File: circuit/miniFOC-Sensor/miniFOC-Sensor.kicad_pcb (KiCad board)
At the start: 2 copper layers, 0 parts

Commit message: Completed PCB drawing of miniFOC sensor board
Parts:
- added C1: 100nF, Capacitor_SMD:C_0402_1005Metric, B.Cu at (154.7, 105.8)
- added C2: 22uF, Capacitor_SMD:C_0603_1608Metric, F.Cu at (150.4, 107.0)
- added C3: 22uF, Capacitor_SMD:C_0603_1608Metric, B.Cu at (154.7, 102.3)
- added J1: Conn_01x05, Connector_JST:JST_GH_SM05B-GHS-TB_1x05-1MP_P1.25mm_Horizontal, F.Cu at (149.8, 115.6)
- added U1: MT6701, Package_SO:SOP-8_3.9x4.9mm_P1.27mm, B.Cu at (149.8, 104.3)
- added U2: XC6206P332MR, Package_TO_SOT_SMD:SOT-23, F.Cu at (149.8, 104.3)
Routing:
- net /SPI_CS: track 0.00 -> 14.3 mm, vias 0 -> 1
- net +5V: track 0.00 -> 13.0 mm
- net /SPI_CLK: track 0.00 -> 12.1 mm, vias 0 -> 1
- net /SPI_MISO: track 0.00 -> 9.94 mm, vias 0 -> 1
- net +3.3V: track 0.00 -> 9.25 mm, vias 0 -> 1
- net GND: vias 0 -> 8
- added copper zone on B.Cu, net GND
- added copper zone on F.Cu, net GND
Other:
- board outline added: 30 x 29 mm
- board text added: "0"
- board text added: "0 mm"
- board text added: "0.01 mm"
- board text added: "0.02"
- board text added: "0.035 mm"
- board text added: "0.2000 mm / 0.2000 mm"
- board text added: "0.3000 mm"
- board text added: "0.91 mm"
- board text added: "1"
- board text added: "1.0000 mm"
- board text added: "2"
- board text added: "29.9726 mm x 28.9824 mm"
- board text added: "3.3"
- board text added: "4.2"
- board text added: "B.Cu"
- board text added: "B.Mask"
- board text added: "B.Paste"
- board text added: "B.Silkscreen"
- board text added: "BOARD CHARACTERISTICS"
- board text added: "Black"
- board text added: "Bottom Silk Screen"
- board text added: "Bottom Solder Mask"
- board text added: "Bottom Solder Paste"
- board text added: "Epsilon R（相对介电常数）"
- board text added: "F.Cu"
- board text added: "F.Mask"
- board text added: "F.Paste"
- board text added: "F.Silkscreen"
- board text added: "FR4"
- board text added: "JLCJLCJLCJLC"
- board text added: "Loss Tangent（损耗角正切）"
- board text added: "None"
- board text added: "Not specified"
- board text added: "Top Silk Screen"
- board text added: "Top Solder Mask"
- board text added: "Top Solder Paste"
- board text added: "White"
- board text added: "copper"
- board text added: "core"
- board text added: "github.com/zhuyan zhen1/minifoc"
- board text added: "miniFOC"
- board text added: "否"
- board text added: "孔最小直径："
- board text added: "层名称"
- board text added: "最小布线/间距："
- board text added: "材料"
- board text added: "板子整体尺寸："
- board text added: "电介质"
- board text added: "电路板厚度："
- board text added: "电镀板边："
- board text added: "类型"
- board text added: "粗细 (mm)"
- board text added: "边缘卡连接器："
- board text added: "邮票孔："
- board text added: "铜层数量："
- board text added: "铜表面处理（镀铜）："
- board text added: "阻抗控制"
- board text added: "颜色"

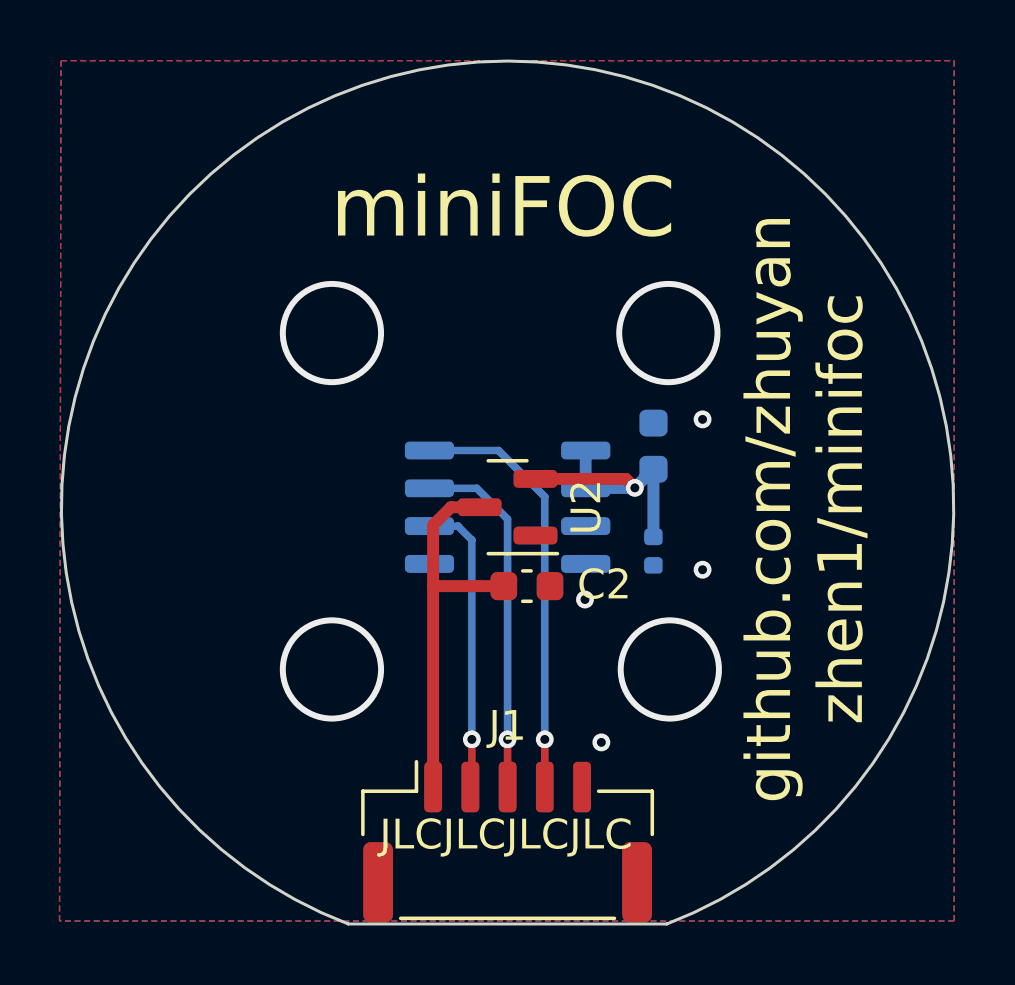
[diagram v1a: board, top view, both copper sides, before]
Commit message: Complete the circuit and PCB design for version 2.0.
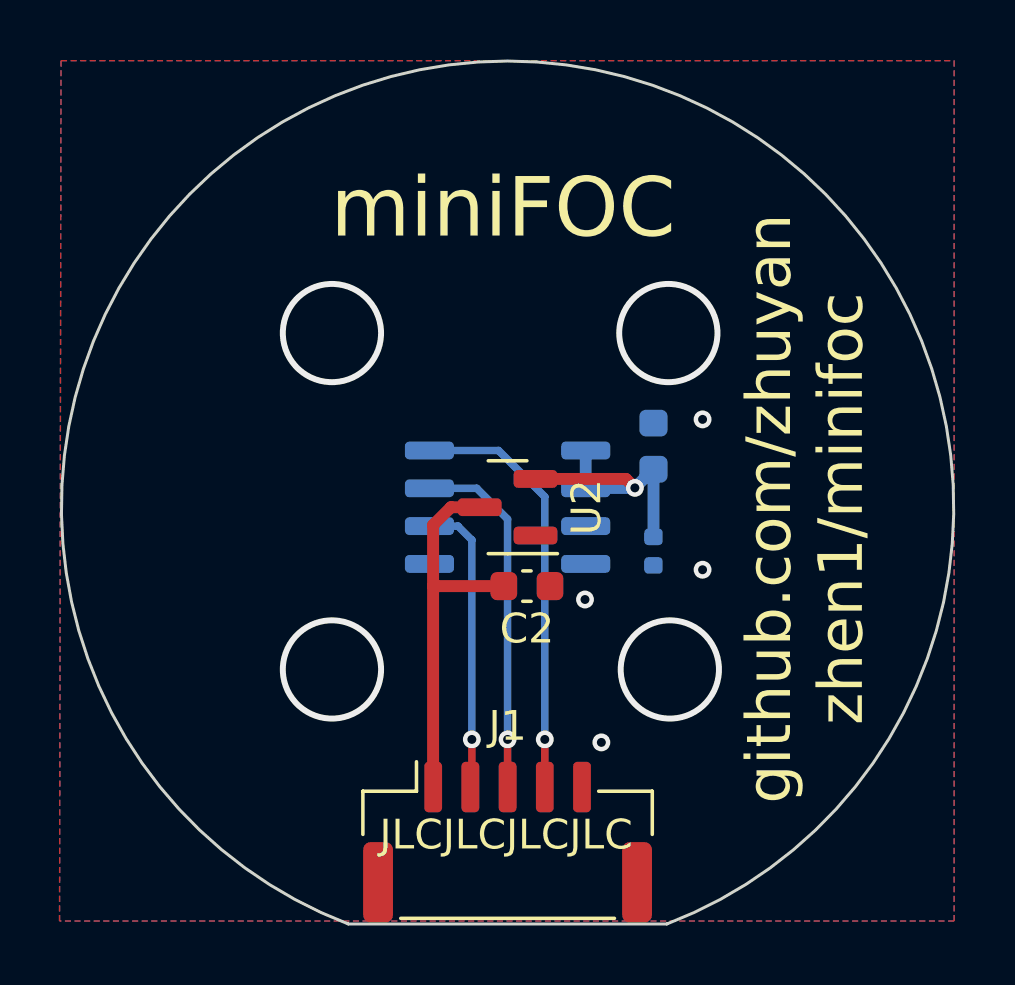
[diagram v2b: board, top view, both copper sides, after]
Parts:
- C1: footprint Capacitor_SMD:C_0402_1005Metric -> Library:C_0402_1005Metric
- C2, C3: footprint Capacitor_SMD:C_0603_1608Metric -> Library:C_0603_1608Metric
- J1: footprint Connector_JST:JST_GH_SM05B-GHS-TB_1x05-1MP_P1.25mm_Horizontal -> Library:JST_GH_SM05B-GHS-TB_1x05-1MP_P1.25mm_Horizontal
- U1: footprint Package_SO:SOP-8_3.9x4.9mm_P1.27mm -> Library:SOP-8_3.9x4.9mm_P1.27mm
- U2: footprint Package_TO_SOT_SMD:SOT-23 -> Library:SOT-23

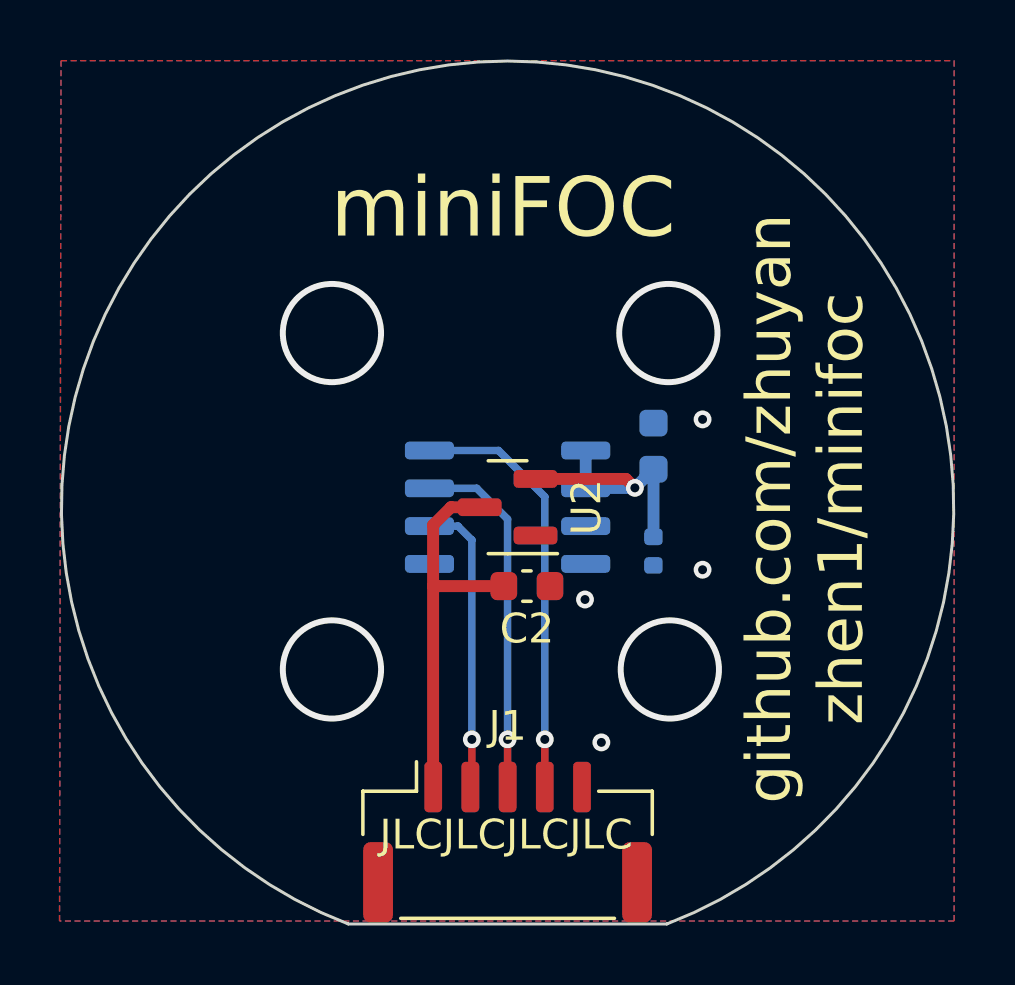
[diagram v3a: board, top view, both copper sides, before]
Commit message: Updated the version number of the sensor board and adjusted the silk screen position in the PCB.
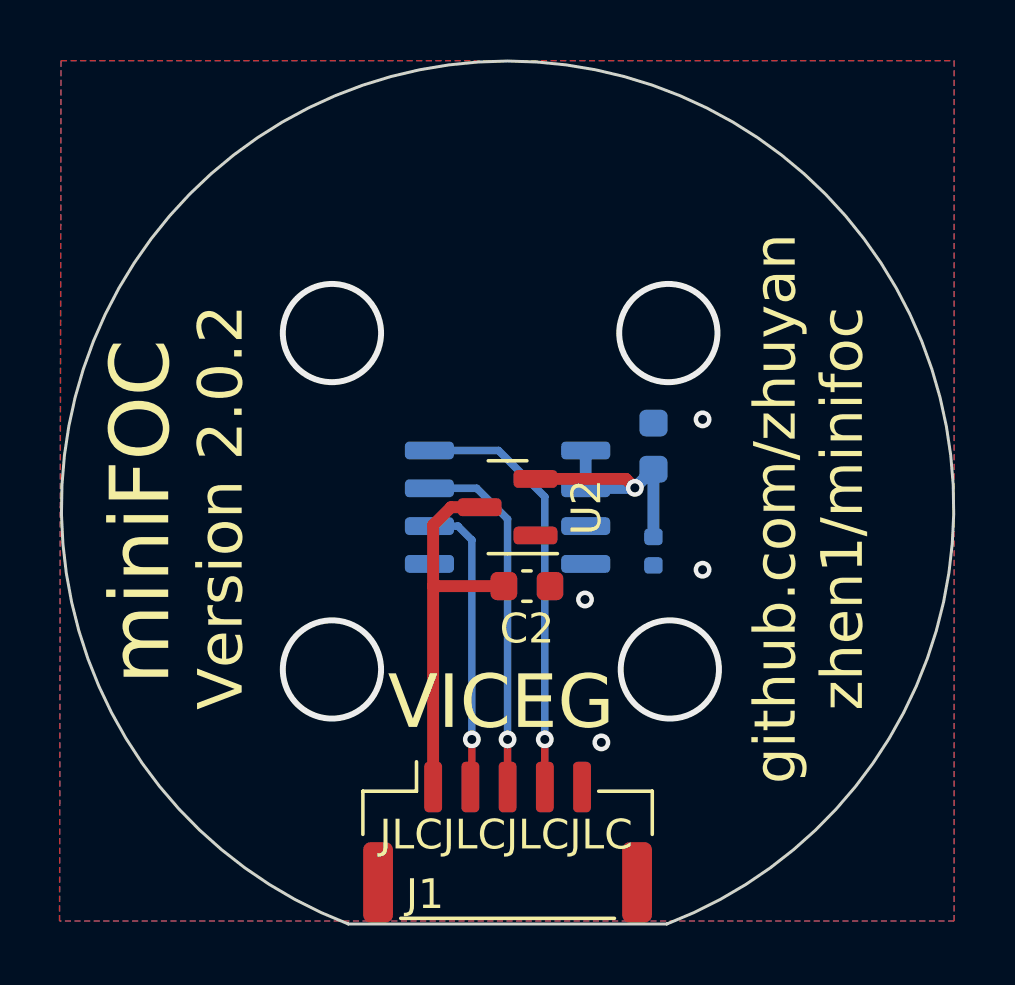
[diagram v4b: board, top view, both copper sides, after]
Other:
- board text added: "VICEG"
- board text added: "Version 2.0.2"
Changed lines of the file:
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@@
   (title_block
     (title "miniFOC-Sensor")
-    (date "2023-06-18")
-    (rev "2.0.1")
+    (date "2023-10-09")
+    (rev "2.0.2")
   )
   (layers
@@
       (viasonmask false)
       (mode 1)
-      (useauxorigin false)
+      (useauxorigin true)
       (hpglpennumber 1)
       (hpglpenspeed 20)
@@
       (outputformat 1)
       (mirror false)
-      (drillshape 1)
+      (drillshape 0)
       (scaleselection 1)
-      (outputdirectory "")
+      (outputdirectory "gerber")
     )
   )
@@
     (property "Sheetname" "")
     (attr smd)
-    (fp_text reference "J1" (at 0 -3.9) (layer "F.SilkS")
+    (fp_text reference "J1" (at -2.775 1.75) (layer "F.SilkS")
         (effects (font (size 1 1) (thickness 0.15)))
     )
@@
     (property "Sheetname" "")
     (attr smd)
-    (fp_text reference "C3" (at 0 1.43 90) (layer "B.SilkS")
+    (fp_text reference "C3" (at 0 -1.475 90) (layer "B.SilkS")
         (effects (font (size 1 1) (thickness 0.15)) (justify mirror))
     )
@@
     (property "Sheetname" "")
     (attr smd)
-    (fp_text reference "C1" (at 0 1.16 90) (layer "B.SilkS")
+    (fp_text reference "C1" (at 0.025 -1.225 90) (layer "B.SilkS")
         (effects (font (size 1 1) (thickness 0.15)) (justify mirror))
     )
@@
   (gr_line (start 42.55 129.89) (end 42.55 170.84)
     (stroke (width 0.1) (type solid)) (layer "F.Fab"))
+  (gr_text "VICEG" (at 145.75 111.95) (layer "F.SilkS")
+    (effects (font (size 1.8 1.8) (thickness 0.3)) (justify left bottom))
+  )
+  (gr_text "Version 2.0.2" (at 140.15 104.35 90) (layer "F.SilkS")
+    (effects (font (size 1.5 1.5) (thickness 0.2)))
+  )
   (gr_text "JLCJLCJLCJLC" (at 149.725 115.35) (layer "F.SilkS")
     (effects (font (size 1 1) (thickness 0.15)))
   )
-  (gr_text "github.com/zhuyan\nzhen1/minifoc" (at 159.775 104.4 90) (layer "F.SilkS")
-    (effects (font (size 1.5 1.5) (thickness 0.25)))
-  )
-  (gr_text "miniFOC" (at 149.625 94.3) (layer "F.SilkS")
+  (gr_text "github.com/zhuyan\nzhen1/minifoc" (at 159.9 104.4 90) (layer "F.SilkS")
+    (effects (font (size 1.4 1.4) (thickness 0.2)))
+  )
+  (gr_text "miniFOC" (at 137.45 104.5 90) (layer "F.SilkS")
     (effects (font (size 2 2) (thickness 0.3)))
   )

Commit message: Modify the appearance of the miniFOC sensor board to use Edge Cuts layer defines holes.
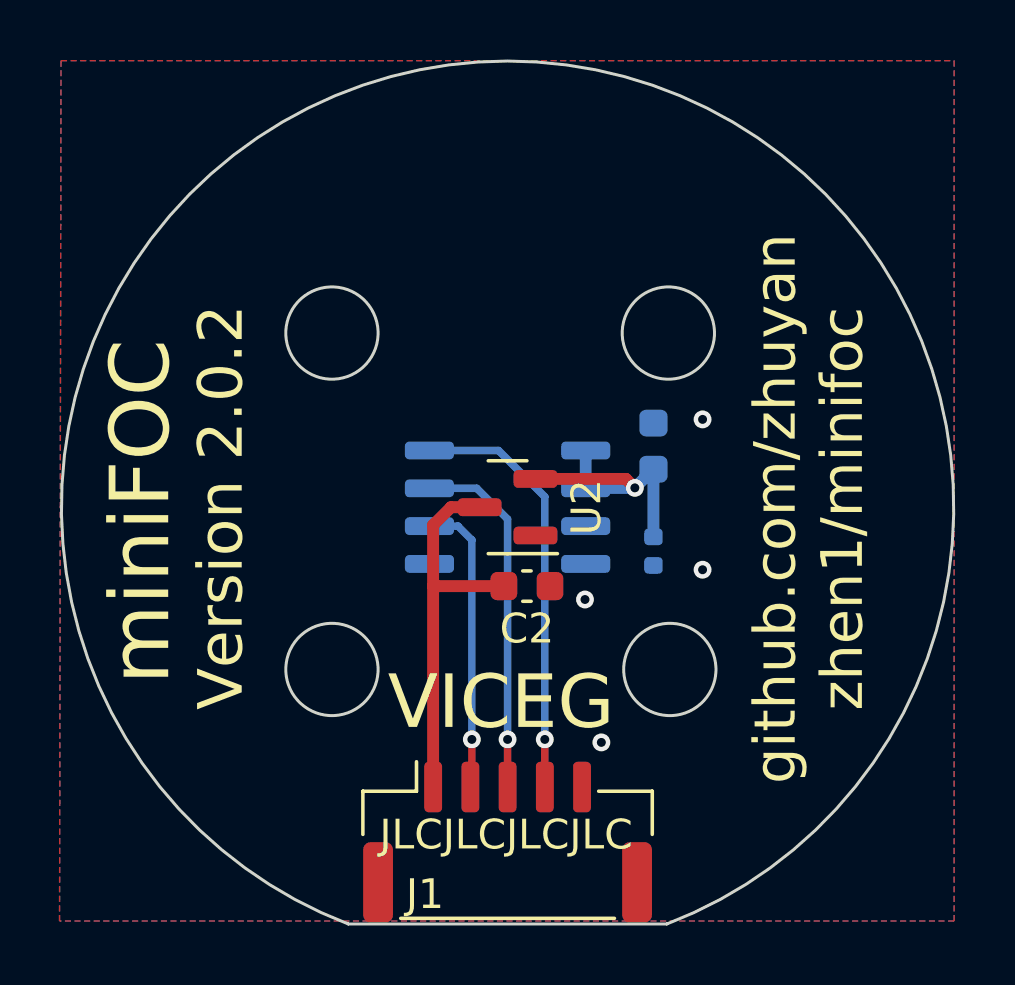
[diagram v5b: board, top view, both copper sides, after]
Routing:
- net GND: vias 8 -> 4
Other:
- outline, holes or cut-outs redrawn
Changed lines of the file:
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@@
     (pad "8" smd roundrect (at 2.625 1.905) (size 1.65 0.6) (layers "B.Cu" "B.Paste" "B.Mask") (roundrect_rratio 0.25)
       (net 5 "/SPI_CS") (pinfunction "CSN") (pintype "input"))
-    (model "${KICAD6_3DMODEL_DIR}/Package_SO.3dshapes/SOP-8_3.9x4.9mm_P1.27mm.wrl"
+    (model "${KICAD7_3DMODEL_DIR}/Package_SO.3dshapes/SOIC-8_3.9x4.9mm_P1.27mm.wrl"
       (offset (xyz 0 0 0))
       (scale (xyz 1 1 1))
@@
   (gr_line (start 144.425 118.35) (end 155.125 118.35)
     (stroke (width 0.1) (type solid)) (layer "Edge.Cuts"))
+  (gr_circle (center 155.225 109.8) (end 156.775 109.8)
+    (stroke (width 0.1) (type default)) (fill none) (layer "Edge.Cuts"))
+  (gr_circle (center 155.175 98.5) (end 156.725 98.5)
+    (stroke (width 0.1) (type default)) (fill none) (layer "Edge.Cuts"))
+  (gr_circle (center 143.875 109.8) (end 145.425 109.8)
+    (stroke (width 0.1) (type default)) (fill none) (layer "Edge.Cuts"))
+  (gr_circle (center 143.875 98.5) (end 145.425 98.5)
+    (stroke (width 0.1) (type default)) (fill none) (layer "Edge.Cuts"))
   (gr_arc (start 144.425 118.35) (mid 149.775 89.362589) (end 155.125 118.35)
     (stroke (width 0.1) (type solid)) (layer "Edge.Cuts"))
@@
   (segment (start 147.275 104.95) (end 147.875 104.35) (width 0.4) (layer "F.Cu") (net 1))
   (segment (start 147.275 113.75) (end 147.275 107) (width 0.4) (layer "F.Cu") (net 1))
-  (via (at 155.225 109.8) (size 3.5) (drill 3.1) (layers "F.Cu" "B.Cu") (free) (net 2))
-  (via (at 143.875 98.5) (size 3.5) (drill 3.1) (layers "F.Cu" "B.Cu") (free) (net 2))
-  (via (at 155.175 98.5) (size 3.5) (drill 3.1) (layers "F.Cu" "B.Cu") (free) (net 2))
   (via (at 152.375 107.45) (size 0.6) (drill 0.3) (layers "F.Cu" "B.Cu") (free) (net 2))
   (via (at 152.925 112.25) (size 0.6) (drill 0.3) (layers "F.Cu" "B.Cu") (free) (net 2))
-  (via (at 143.875 109.8) (size 3.5) (drill 3.1) (layers "F.Cu" "B.Cu") (free) (net 2))
   (via (at 156.325 101.4) (size 0.6) (drill 0.3) (layers "F.Cu" "B.Cu") (free) (net 2))
   (via (at 156.325 106.45) (size 0.6) (drill 0.3) (layers "F.Cu" "B.Cu") (free) (net 2))
